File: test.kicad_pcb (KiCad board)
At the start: 2 copper layers, 5 parts

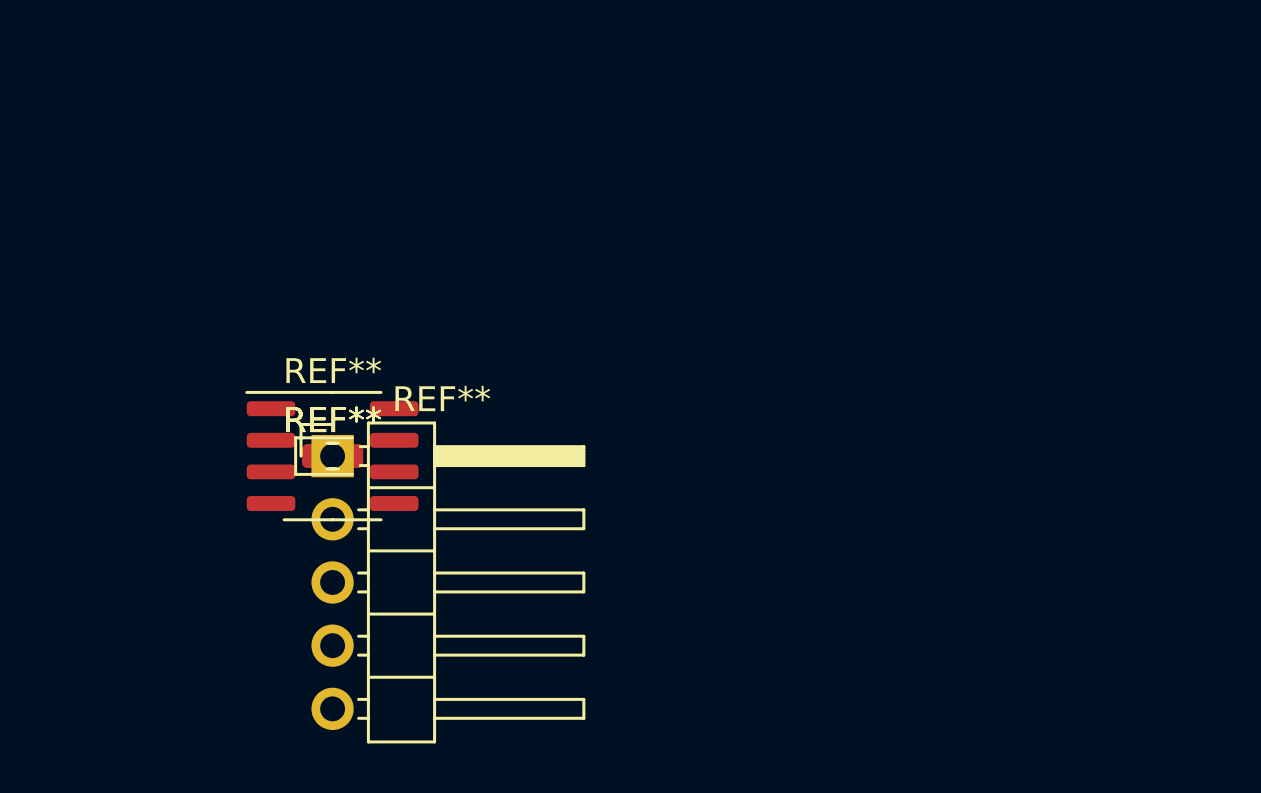
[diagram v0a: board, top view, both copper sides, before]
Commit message: #2 fix error: 替换正则模式为首尾匹配，解决fp_name部分缺失问题
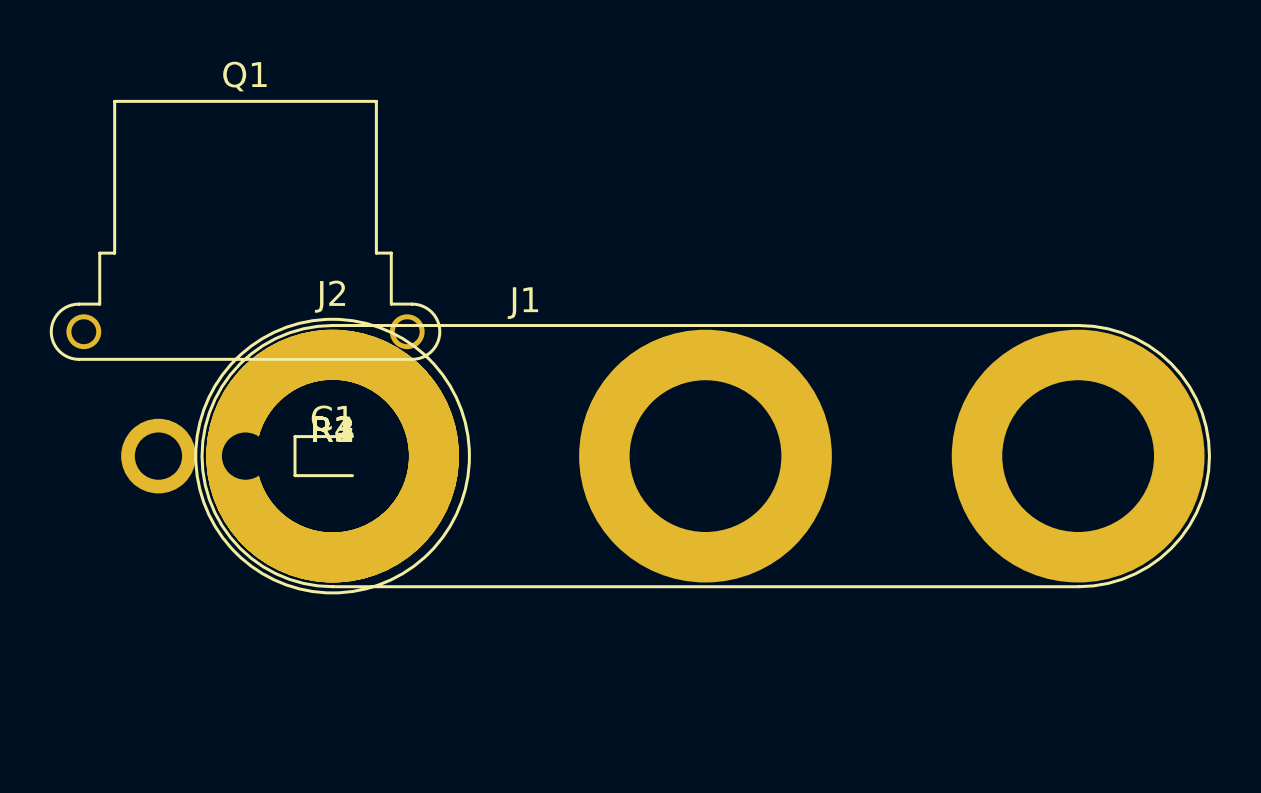
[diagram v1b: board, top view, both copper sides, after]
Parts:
- removed REF**: C_0603_1608Metric, Capacitor_SMD:C_0603_1608Metric
- removed REF**: LED_0603_1608Metric, LED_SMD:LED_0603_1608Metric
- removed REF**: PinHeader_1x05_P2.54mm_Horizontal, Connector_PinHeader_2.54mm:PinHeader_1x05_P2.54mm_Horizontal
- removed REF**: R_0603_1608Metric, Resistor_SMD:R_0603_1608Metric
- removed REF**: SOIC-8_3.9x4.9mm_P1.27mm, Package_SO:SOIC-8_3.9x4.9mm_P1.27mm
- added C1: CP_EIA-1608-10_AVX-L, Capacitor_Tantalum_SMD:CP_EIA-1608-10_AVX-L, F.Cu at (0.00, 0.00)
- added J1: Banana_Jack_3Pin, Connector:Banana_Jack_3Pin, F.Cu at (0.00, 0.00)
- added J2: Banana_Jack_1Pin, Connector:Banana_Jack_1Pin, F.Cu at (0.00, 0.00)
- added Q1: AMASS_MR30PW-FB_1x03_P3.50mm_Horizontal, Connector_AMASS:AMASS_MR30PW-FB_1x03_P3.50mm_Horizontal, F.Cu at (0.00, 0.00)
- added R1, R2, R3, R4: R_0201_0603Metric, Resistor_SMD:R_0201_0603Metric, F.Cu at (0.00, 0.00)

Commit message: #5 fix error: 修复net网络匹配错误
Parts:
- C1: value CP_EIA-1608-10_AVX-L -> 1uf
- J1: value Banana_Jack_3Pin -> Conn_01x03
- J2: value Banana_Jack_1Pin -> Conn_01x01
- Q1: value AMASS_MR30PW-FB_1x03_P3.50mm_Horizontal -> PNP
- R1: value R_0201_0603Metric -> 10R
- R2: value R_0201_0603Metric -> 10K
- R3: value R_0201_0603Metric -> 1K
- R4: value R_0201_0603Metric -> 5R
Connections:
- C1 pad 1: (no net) -> Net-(Q1-B)
- C1 pad 2: (no net) -> /signal
- J1 pad 1: (no net) -> /signal
- J1 pad 2: (no net) -> GND
- J1 pad 3: (no net) -> VCC
- J2 pad 1: (no net) -> /out
- Q1 pad 1: (no net) -> Net-(Q1-C)
- Q1 pad 2: (no net) -> Net-(Q1-B)
- Q1 pad 3: (no net) -> GND
- R1 pad 1: (no net) -> Net-(Q1-B)
- R1 pad 2: (no net) -> GND
- R2 pad 1: (no net) -> /out
- R2 pad 2: (no net) -> Net-(Q1-C)
- R3 pad 1: (no net) -> VCC
- R3 pad 2: (no net) -> Net-(Q1-C)
- R4 pad 1: (no net) -> VCC
- R4 pad 2: (no net) -> Net-(Q1-B)
